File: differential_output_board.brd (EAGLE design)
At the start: 100 x 50 mm, 26 parts, among them IC1 TJA1057

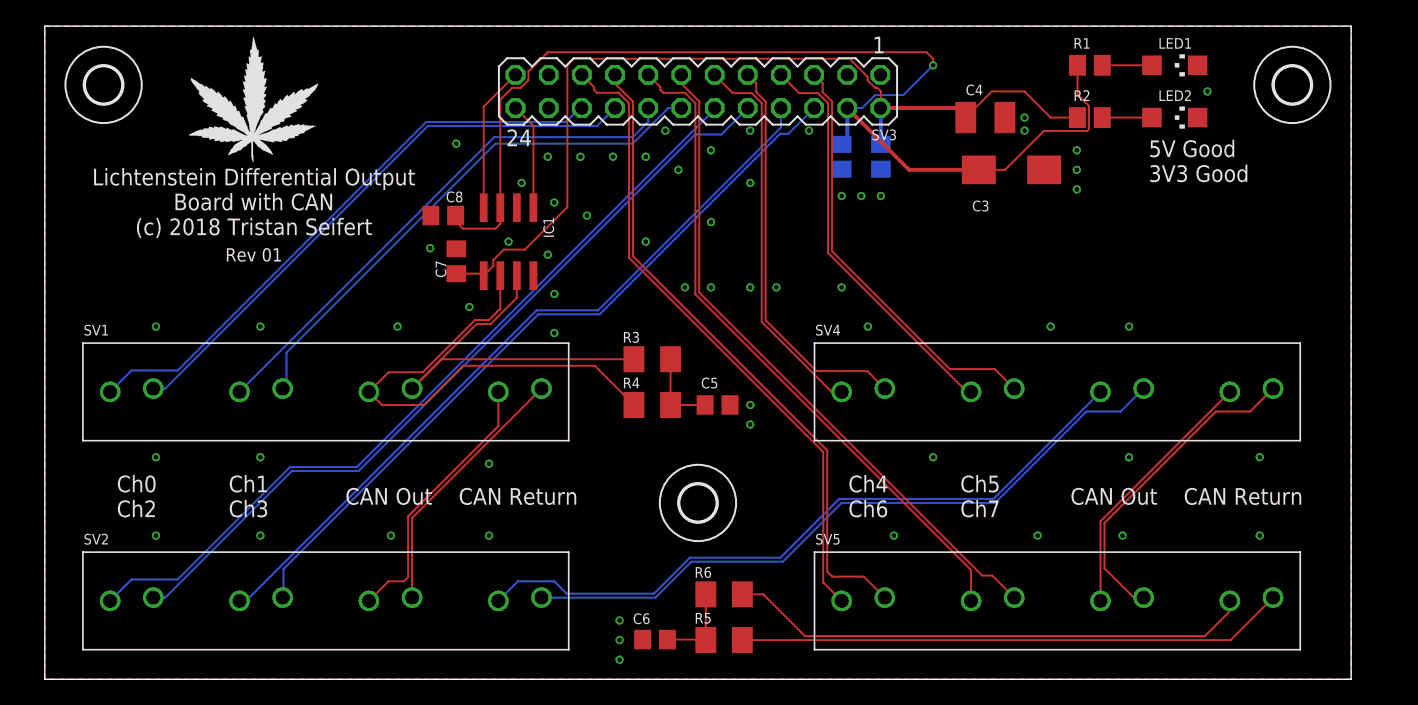
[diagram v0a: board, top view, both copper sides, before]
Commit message: added footprints for termination resistors on output connection board
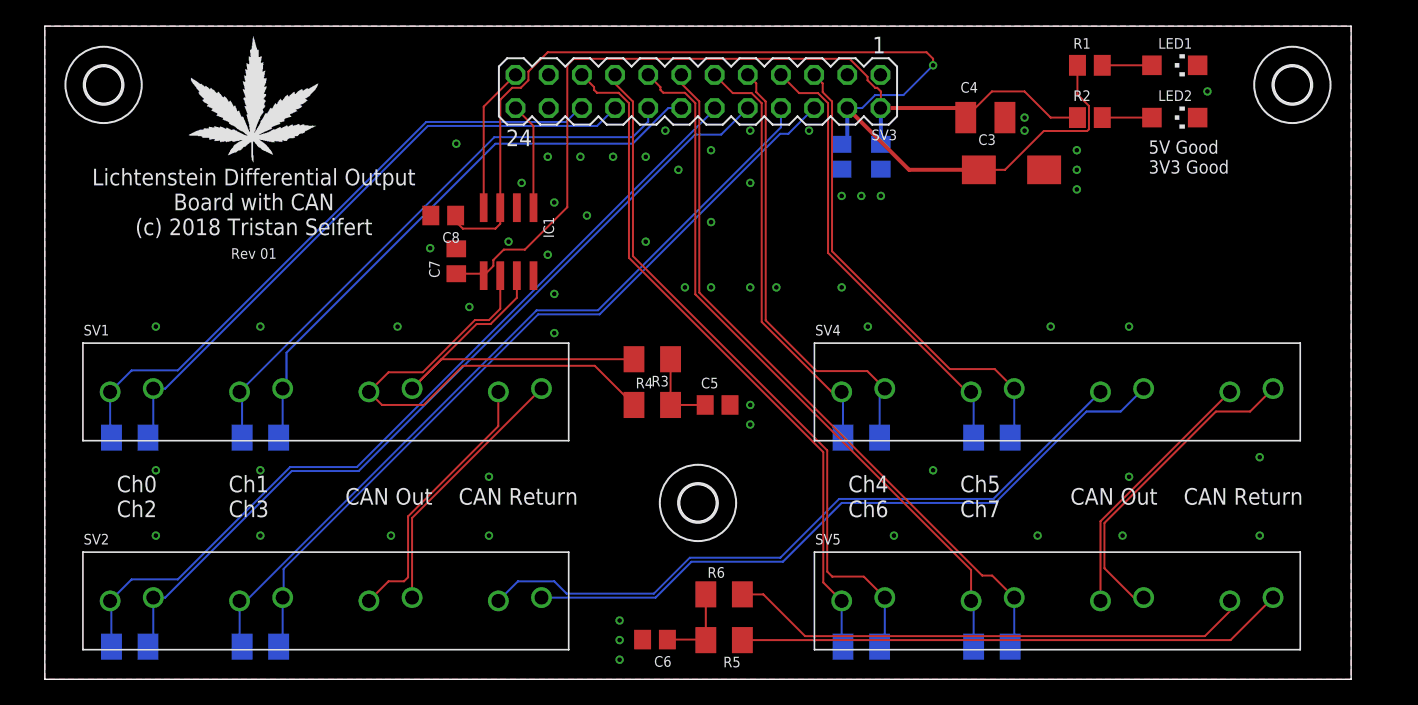
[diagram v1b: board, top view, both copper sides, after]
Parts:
- added R10, R11, R12, R13, R14, R7, R8, R9: 100R, rcl:M1206
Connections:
- net OUT0_N: now also R7.1
- net OUT0_P: now also R7.2
- net OUT1_N: now also R8.1
- net OUT1_P: now also R8.2
- net OUT2_N: now also R9.1
- net OUT2_P: now also R9.2
- net OUT3_N: now also R10.1
- net OUT3_P: now also R10.2
- net OUT4_N: now also R11.1
- net OUT4_P: now also R11.2
- net OUT5_N: now also R12.1
- net OUT5_P: now also R12.2
- net OUT6_N: now also R13.1
- net OUT6_P: now also R13.2
- net OUT7_N: now also R14.1
- net OUT7_P: now also R14.2
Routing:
- net OUT5_P: track 30.6 -> 34.6 mm
- net OUT7_P: track 50.0 -> 53.9 mm
- net OUT0_P: track 44.2 -> 48.2 mm
- net OUT2_P: track 61.0 -> 65.0 mm
- net OUT1_P: track 40.9 -> 44.7 mm
- net OUT4_P: track 32.4 -> 36.3 mm
- net OUT3_P: track 57.4 -> 61.3 mm
- net OUT6_P: track 51.0 -> 54.9 mm
- net OUT1_N: track 40.9 -> 44.5 mm
- net OUT4_N: track 31.3 -> 34.9 mm
- net OUT3_N: track 57.9 -> 61.5 mm
- net OUT6_N: track 51.5 -> 55.1 mm
- net OUT7_N: track 49.5 -> 53.0 mm
- net OUT5_N: track 29.6 -> 33.1 mm
- net OUT0_N: track 45.1 -> 48.7 mm
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
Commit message: submitted rev 1 of output and led boards to board house
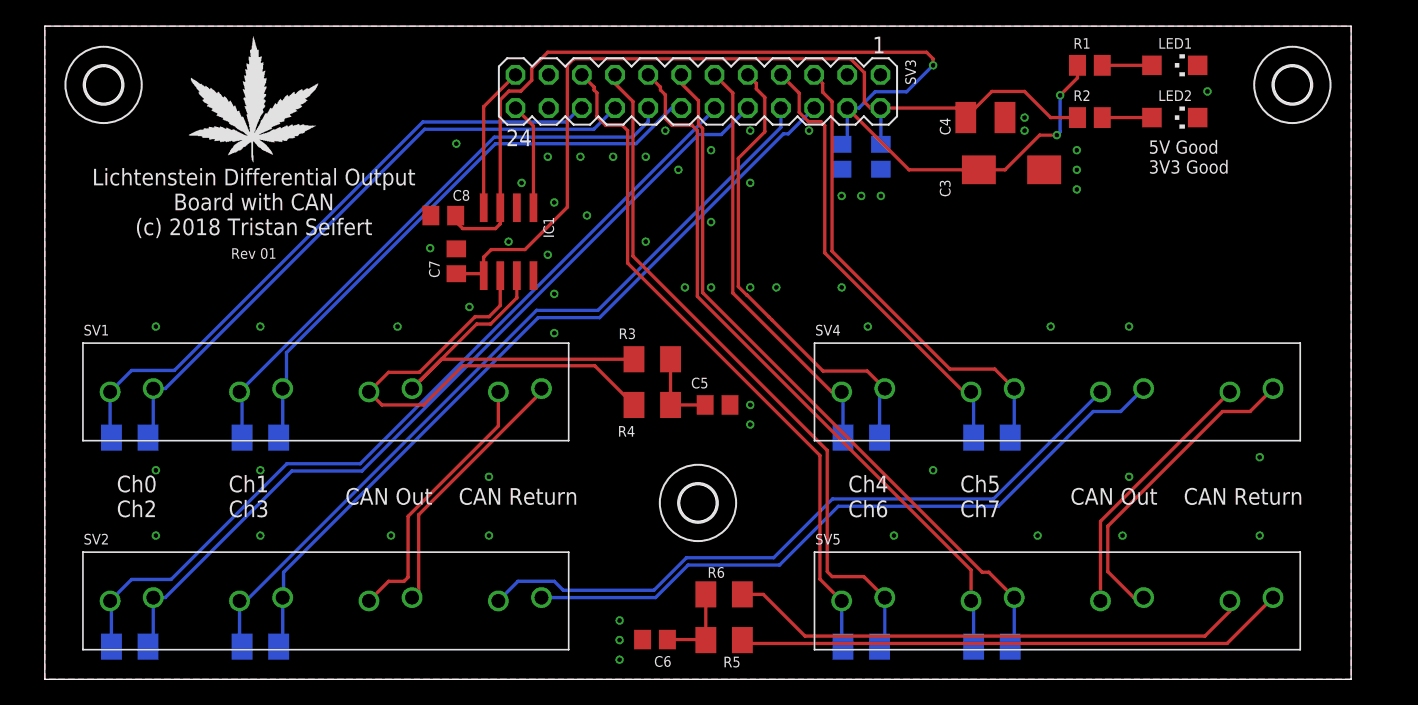
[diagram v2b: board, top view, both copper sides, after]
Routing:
- net +5V: track 87.4 -> 85.6 mm, vias 1 -> 3
- net OUT5_P: track 34.6 -> 36.0 mm
- net +3V3: track 68.4 -> 69.3 mm
- net OUT5_N: track 33.1 -> 32.3 mm
- net CANH_3: track 24.6 -> 24.1 mm

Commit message: rev2 of differential output board (fix capacitor footprint)
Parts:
- C3: device rcl:CT6032 -> rcl:SMC_D
- moved WEED1 1.27 mm to (9.73, 39.5)
- moved C3 0.51 mm to (74.0, 38.5)
- moved C4 0.25 mm to (72.0, 43.3)
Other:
- board text added: "Rev 02"
- board text removed: "Rev 01"
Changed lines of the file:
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@@
 <text x="61.5" y="14" size="1.27" layer="25" font="vector" ratio="12" align="center-left">Ch4           Ch5
 Ch6           Ch7</text>
-<text x="16" y="34" size="1.27" layer="25" font="vector" ratio="12" align="bottom-center">Lichtenstein Differential Output
+<text x="83.564" y="29.174" size="1.4224" layer="25" font="vector" ratio="12" align="bottom-center">Lichtenstein Differential Output
 Board with CAN
 (c) 2018 Tristan Seifert</text>
@@
 <text x="23" y="14" size="1.27" layer="25" font="vector" ratio="12" align="center-left">CAN Out    CAN Return</text>
 <text x="78.5" y="14" size="1.27" layer="25" font="vector" ratio="12" align="center-left">CAN Out    CAN Return</text>
-<text x="16" y="33" size="0.8128" layer="25" font="vector" ratio="10" align="top-center">Rev 01</text>
+<text x="9.65" y="38.334" size="1.27" layer="25" font="vector" ratio="10" align="top-left">Rev 02</text>
 </plain>
 <attributes>
@@
 <attribute name="SPICEPREFIX" value="C" x="64" y="40" size="1.778" layer="28" rot="MR270" display="off"/>
 </element>
-<element name="C4" library="rcl" library_urn="urn:adsk.eagle:library:334" package="SMC_B" package3d_urn="urn:adsk.eagle:package:25920/1" value="10µF" x="72" y="43" smashed="yes">
-<attribute name="MOUSER" value="581-TAJB106K020RNJV" x="72" y="43" size="1.778" layer="27" display="off"/>
-<attribute name="NAME" x="69.331" y="41.647" size="0.8128" layer="25" font="vector" ratio="10" rot="R90"/>
-<attribute name="SPICEPREFIX" value="C" x="72" y="43" size="1.778" layer="27" display="off"/>
+<element name="C4" library="rcl" library_urn="urn:adsk.eagle:library:334" package="SMC_B" package3d_urn="urn:adsk.eagle:package:25920/1" value="10µF" x="72" y="43.254" smashed="yes">
+<attribute name="MOUSER" value="581-TAJB106K020RNJV" x="72" y="43.254" size="1.778" layer="27" display="off"/>
+<attribute name="NAME" x="69.331" y="41.901" size="0.8128" layer="25" font="vector" ratio="10" rot="R90"/>
+<attribute name="SPICEPREFIX" value="C" x="72" y="43.254" size="1.778" layer="27" display="off"/>
 </element>
 <element name="C1" library="rcl" library_urn="urn:adsk.eagle:library:334" package="C0805" package3d_urn="urn:adsk.eagle:package:23617/2" value="100nF" x="61" y="40" smashed="yes" rot="MR270">
@@
 <attribute name="SPICEPREFIX" value="C" x="30.5" y="35.5" size="1.778" layer="27" rot="R180" display="off"/>
 </element>
-<element name="C3" library="rcl" library_urn="urn:adsk.eagle:library:334" package="CT6032" package3d_urn="urn:adsk.eagle:package:23305/2" value="47µF" x="74" y="39" smashed="yes">
-<attribute name="MOUSER" value="581-TAJD476M016RNJV" x="74" y="39" size="1.778" layer="27" display="off"/>
-<attribute name="NAME" x="69.331" y="36.916" size="0.8128" layer="25" font="vector" ratio="10" rot="R90"/>
-<attribute name="SPICEPREFIX" value="C" x="74" y="39" size="1.778" layer="27" display="off"/>
+<element name="C3" library="rcl" library_urn="urn:adsk.eagle:library:334" package="SMC_D" package3d_urn="urn:adsk.eagle:package:25923/1" value="47µF" x="74" y="38.492" smashed="yes">
+<attribute name="MOUSER" value="581-TAJD476M016RNJV" x="74" y="38.492" size="1.778" layer="27" display="off"/>
+<attribute name="NAME" x="69.331" y="36.408" size="0.8128" layer="25" font="vector" ratio="10" rot="R90"/>
+<attribute name="SPICEPREFIX" value="C" x="74" y="38.492" size="1.778" layer="27" display="off"/>
 </element>
 <element name="C5" library="rcl" library_urn="urn:adsk.eagle:library:334" package="C0805" package3d_urn="urn:adsk.eagle:package:23617/2" value="4.7nF" x="51.5" y="21" smashed="yes">
@@
 <attribute name="NAME" x="58.968" y="10.318" size="0.8128" layer="25" font="vector" ratio="10"/>
 </element>
-<element name="WEED1" library="lichtenstein_onion" package="DOINK" value="WEED" x="11" y="39.5" smashed="yes"/>
+<element name="WEED1" library="lichtenstein_onion" package="DOINK" value="WEED" x="9.73" y="39.5" smashed="yes"/>
 <element name="H1" library="holes" library_urn="urn:adsk.eagle:library:237" package="2,8" package3d_urn="urn:adsk.eagle:package:14271/1" value="MOUNT-HOLE2.8" x="4.5" y="45.5" smashed="yes"/>
 <element name="H2" library="holes" library_urn="urn:adsk.eagle:library:237" package="2,8" package3d_urn="urn:adsk.eagle:package:14271/1" value="MOUNT-HOLE2.8" x="95.5" y="45.5" smashed="yes"/>
@@
 <wire x1="64" y1="40.95" x2="64" y2="43.73" width="0.254" layer="16"/>
 <wire x1="64" y1="43.73" x2="63.97" y2="43.73" width="0.254" layer="16"/>
-<wire x1="63.97" y1="43.73" x2="69.77" y2="43.73" width="0.254" layer="1"/>
-<wire x1="69.77" y1="43.73" x2="70.5" y2="43" width="0.254" layer="1"/>
+<wire x1="63.97" y1="43.73" x2="70.024" y2="43.73" width="0.254" layer="1"/>
+<wire x1="70.024" y1="43.73" x2="70.5" y2="43.254" width="0.254" layer="1"/>
 <wire x1="79.05" y1="43" x2="77" y2="43" width="0.254" layer="1"/>
 <wire x1="77" y1="43" x2="75" y2="45" width="0.254" layer="1"/>
-<wire x1="75" y1="45" x2="72.5" y2="45" width="0.254" layer="1"/>
-<wire x1="72.5" y1="45" x2="70.5" y2="43" width="0.254" layer="1"/>
+<wire x1="75" y1="45" x2="72.246" y2="45" width="0.254" layer="1"/>
+<wire x1="72.246" y1="45" x2="70.5" y2="43.254" width="0.254" layer="1"/>
 <wire x1="33.595" y1="30.9" x2="33.445" y2="31.05" width="0.254" layer="1"/>
 <wire x1="33.445" y1="31.05" x2="31.5" y2="31.05" width="0.254" layer="1"/>
@@
 <via x="39" y="26.5" extent="1-16" drill="0.35"/>
 <via x="54" y="21" extent="1-16" drill="0.35"/>
-<via x="75" y="43" extent="1-16" drill="0.35"/>
-<via x="79" y="39" extent="1-16" drill="0.35"/>
+<via x="75.254" y="43" extent="1-16" drill="0.35"/>
+<via x="79.254" y="39" extent="1-16" drill="0.35"/>
 <via x="29.5" y="33" extent="1-16" drill="0.35"/>
 <via x="31.5" y="41" extent="1-16" drill="0.35"/>
@@
 <via x="44" y="1.5" extent="1-16" drill="0.35"/>
 <via x="54" y="19.5" extent="1-16" drill="0.35"/>
-<via x="79" y="40.5" extent="1-16" drill="0.35"/>
-<via x="79" y="37.5" extent="1-16" drill="0.35"/>
-<via x="75" y="42" extent="1-16" drill="0.35"/>
+<via x="79.254" y="40.5" extent="1-16" drill="0.35"/>
+<via x="79.254" y="37.5" extent="1-16" drill="0.35"/>
+<via x="75.254" y="42" extent="1-16" drill="0.35"/>
+<via x="75.19" y="43.826" extent="1-16" drill="0.35"/>
 </signal>
 <signal name="OUT3_N">
@@
 <wire x1="61" y1="40.95" x2="61.43" y2="41.38" width="0.254" layer="16"/>
 <wire x1="61.43" y1="41.38" x2="61.43" y2="43.73" width="0.254" layer="16"/>
-<wire x1="61.43" y1="43.73" x2="66.16" y2="39" width="0.254" layer="1"/>
-<wire x1="66.16" y1="39" x2="71.5" y2="39" width="0.254" layer="1"/>
-<wire x1="73.5" y1="39" x2="71.5" y2="39" width="0.254" layer="1"/>
-<wire x1="76.156" y1="41.656" x2="73.5" y2="39" width="0.254" layer="1"/>
+<wire x1="61.43" y1="43.73" x2="66.668" y2="38.492" width="0.254" layer="1"/>
+<wire x1="66.668" y1="38.492" x2="70.85" y2="38.492" width="0.254" layer="1"/>
+<wire x1="72.992" y1="38.492" x2="70.85" y2="38.492" width="0.254" layer="1"/>
+<wire x1="76.156" y1="41.656" x2="72.992" y2="38.492" width="0.254" layer="1"/>
 <wire x1="34.865" y1="36.1" x2="34.865" y2="44.365" width="0.254" layer="1"/>
 <wire x1="67.5" y1="48" x2="68" y2="47.5" width="0.254" layer="1"/>
